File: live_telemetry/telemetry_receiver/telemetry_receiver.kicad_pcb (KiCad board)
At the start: 2 copper layers, 52.5 x 30.7 mm, 20 parts, among them J1 Conn_Coaxial, J2 Programming Header, J3 USB_A, U1 PIC16LF1455, U2 RFM95W, U3 AP2114H-3.3

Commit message: Address Aaron's comments on initial component layout
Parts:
- J1: footprint canhw_footprints:AmphenolRF_coaxial_conn_901-10510-2 -> canhw_footprints:RF_connector_SMA_3-1478978-1
- moved D3 10.7 mm to (124.3, 79.7), turned to 180 degrees
- moved R2 9.95 mm to (124.4, 76.3), turned to 180 degrees
- moved D2 8.03 mm to (131.6, 79.6), turned to 180 degrees
- moved R1 6.98 mm to (131.7, 76.3), turned to 180 degrees
- moved J1 5.87 mm to (151.8, 98.5)
- moved D1 5.61 mm to (138.9, 79.6), turned to 180 degrees
- moved J3 4.67 mm to (104.1, 88.5)
- moved J2 4.42 mm to (146.0, 76.4)
- moved R4 4.03 mm to (139.0, 76.3), turned to 180 degrees
- moved U2 3.80 mm to (128.1, 91.5)
- moved C3 1.69 mm to (144.3, 91.5)
- moved C1 1.61 mm to (140.3, 91.4)
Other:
- board size 52.5 x 30.7 mm -> 48.6 x 28 mm

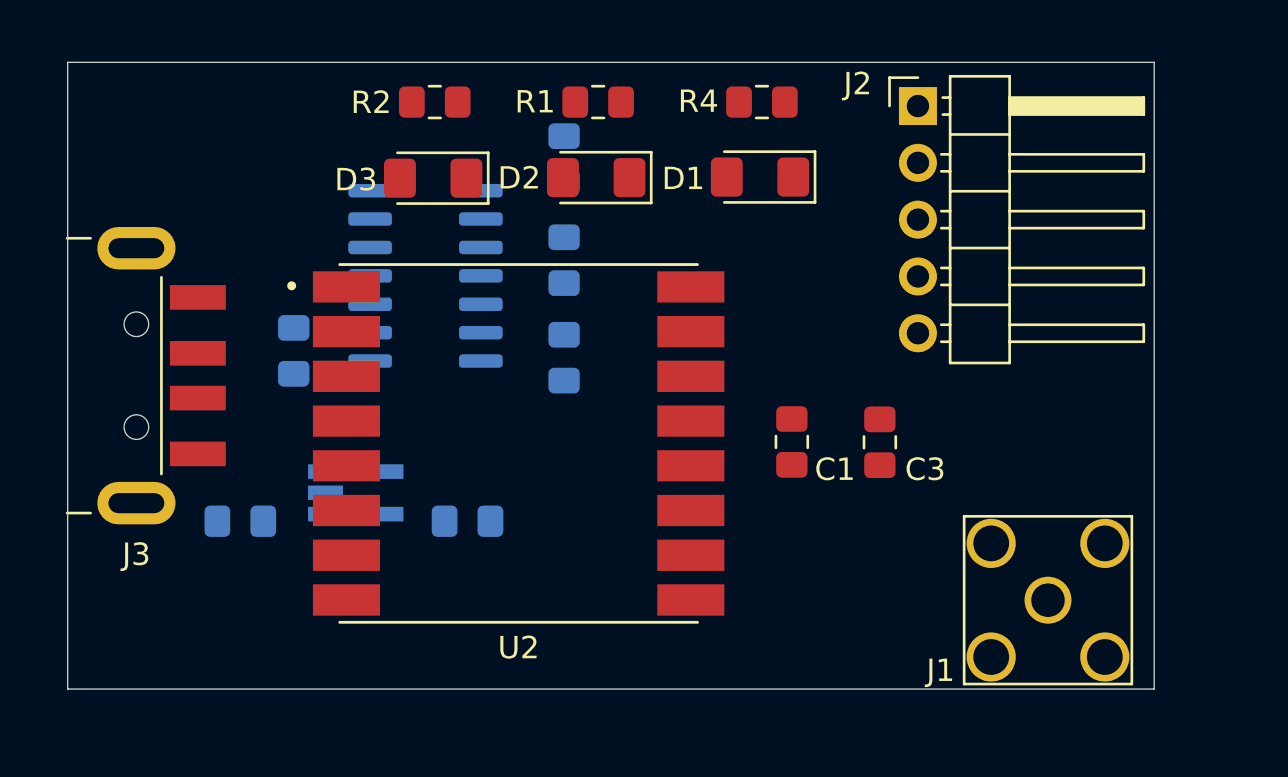
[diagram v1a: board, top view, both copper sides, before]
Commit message: Add initial trace routing
Note:
-LED colours still need to be added
-Waterloo Rocketry logo needs to be added with the board name and
my name on the right side of the board
-Copper pours will be added next commit
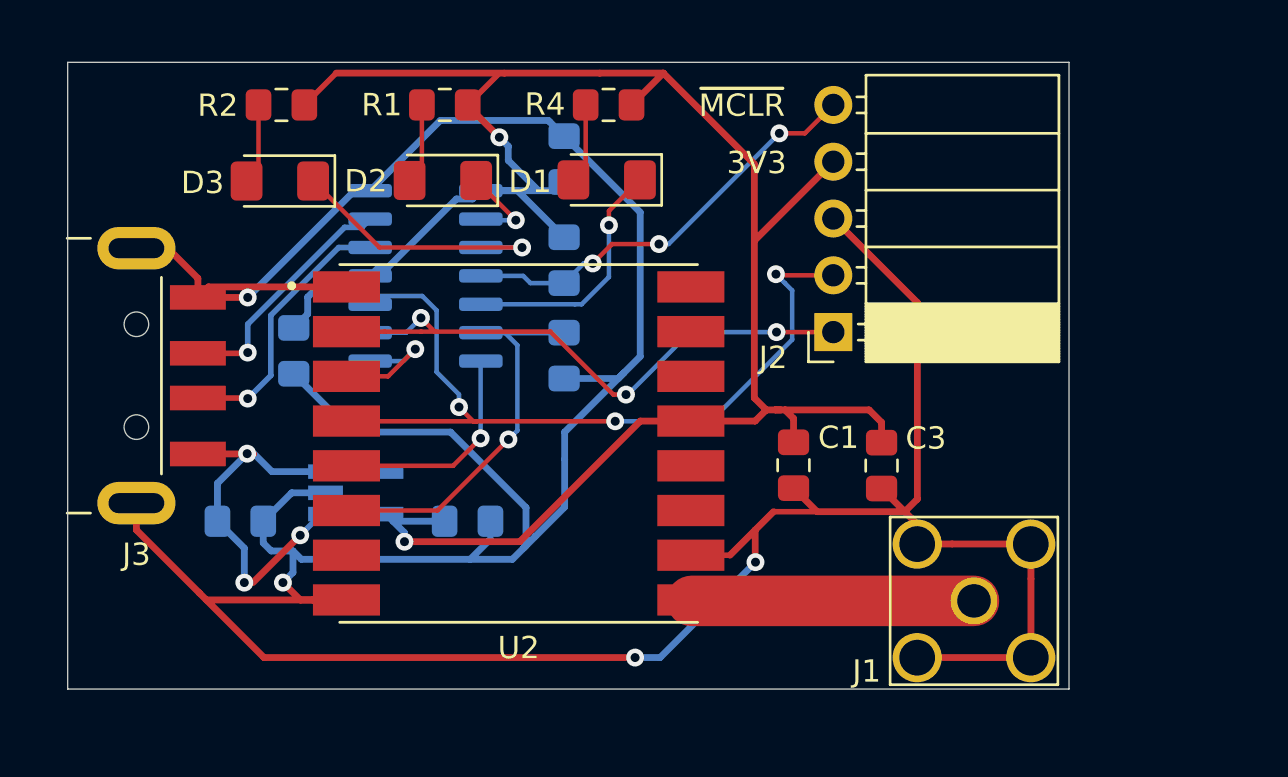
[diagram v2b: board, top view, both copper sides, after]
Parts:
- J2: footprint Connector_PinHeader_2.54mm:PinHeader_1x05_P2.54mm_Horizontal -> Connector_PinSocket_2.54mm:PinSocket_1x05_P2.54mm_Horizontal
- moved J2 10.8 mm to (142.2, 86.5), turned to 180 degrees
- moved D1 6.86 mm to (132.1, 79.7)
- moved R2 6.86 mm to (117.5, 76.4)
- moved R4 6.86 mm to (132.1, 76.4)
- moved D3 6.86 mm to (117.4, 79.8)
- moved D2 6.86 mm to (124.7, 79.8)
- moved R1 6.86 mm to (124.8, 76.4)
- moved J1 3.31 mm to (148.5, 98.6)
- moved C1 1.04 mm to (140.4, 92.5), turned to 270 degrees
- moved C3 1.04 mm to (144.3, 92.5), turned to 270 degrees
- moved R5 0.09 mm to (130.1, 87.6)
- turned R3 to 270 degrees
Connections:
- J2 pad 1: /ISCPCLK -> /ICSPCLK
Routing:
- net GND: track 0.00 -> 183.3 mm, vias 0 -> 4
- net +3V3: track 0.00 -> 98.9 mm, vias 0 -> 2
- net /ICSPDAT: track 0.00 -> 36.4 mm, vias 0 -> 3
- net /ICSPCLK: track 0.00 -> 27.6 mm, vias 0 -> 3
- net /~MCLR: track 0.00 -> 19.2 mm, vias 0 -> 3
- net /RESET: track 0.00 -> 18.5 mm, vias 0 -> 1
- net +5V: track 0.00 -> 17.8 mm, vias 0 -> 3
- net Net-(AE1-Pad1): track 0.00 -> 12.7 mm
- net Net-(D3-Pad1): track 0.00 -> 12.4 mm, vias 0 -> 1
- net /USB_D-: track 0.00 -> 12.1 mm, vias 0 -> 1
- net Net-(D1-Pad1): track 0.00 -> 11.2 mm, vias 0 -> 1
- net /USB_D+: track 0.00 -> 10.9 mm, vias 0 -> 1
- net /~SS: track 0.00 -> 9.97 mm, vias 0 -> 1
- net /MOSI: track 0.00 -> 5.82 mm, vias 0 -> 1
- net Net-(D2-Pad1): track 0.00 -> 4.10 mm, vias 0 -> 1
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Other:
- board size 48.6 x 28 mm -> 44.8 x 28 mm
- net class Default: trace_width 0.25 -> 0.2032
- net class Power added: clearance 0.2, trace_width 0.3048, via_dia 0.8, via_drill 0.4
- board text added: "3V3"
- board text added: "~MCLR"

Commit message: Add copper pours and address Jared's comments
Note:
-Still haven't fixed CAN TX/RX lines running through OSC1&2
-Still need to add team logo
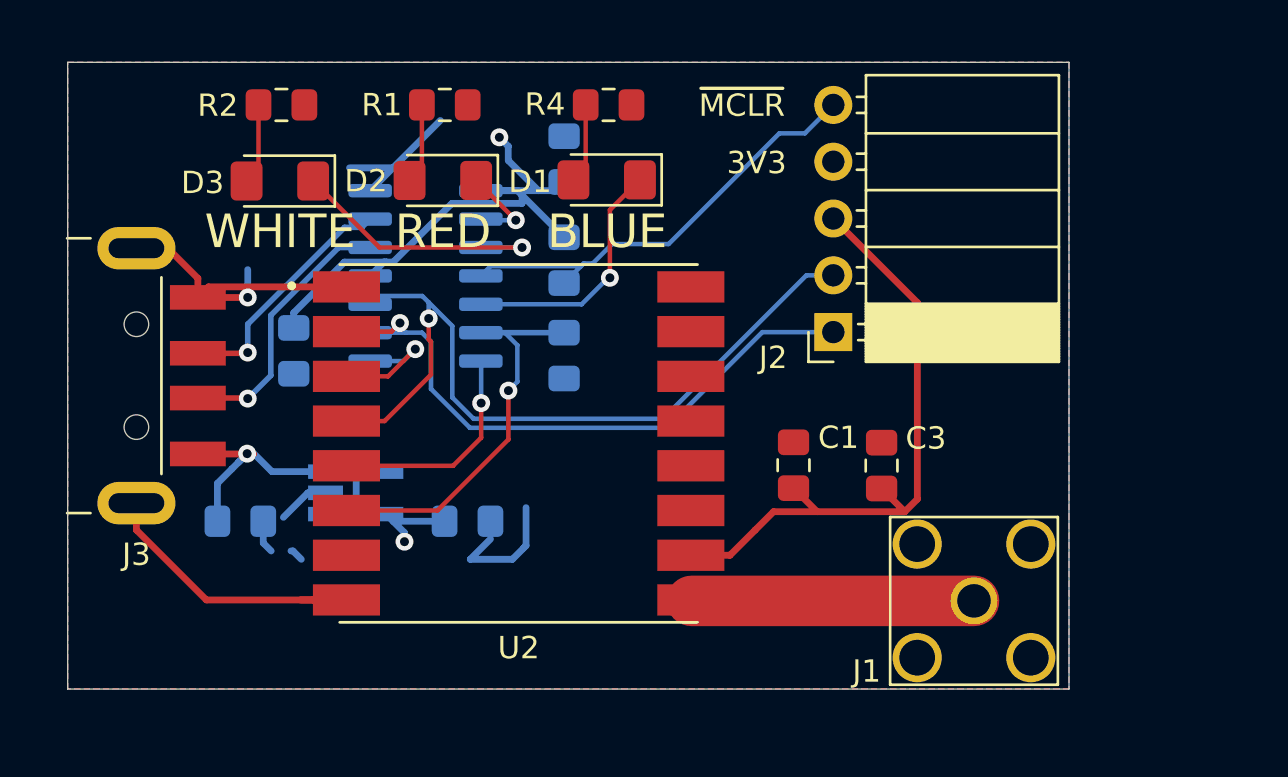
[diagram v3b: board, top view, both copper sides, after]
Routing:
- net GND: track 183.3 -> 77.6 mm, vias 4 -> 1
- net +3V3: track 98.9 -> 30.2 mm
- net +5V: track 17.8 -> 14.7 mm, vias 3 -> 1
- net /ICSPCLK: track 27.6 -> 28.6 mm, vias 3 -> 1
- net /ICSPDAT: track 36.4 -> 35.6 mm, vias 3 -> 1
- net /~MCLR: track 19.2 -> 20.0 mm, vias 3 -> 0
- added copper zone on F.Cu, net +3V3
- added copper zone on B.Cu, net GND
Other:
- board text added: "BLUE"
- board text added: "RED"
- board text added: "WHITE"

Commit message: Address Aaron's comments
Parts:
- moved C6 1.54 mm to (127.2, 95.8), turned to 270 degrees
- moved C5 1.38 mm to (114.6, 95.8), turned to 270 degrees
- moved C2 1.22 mm to (131.4, 78.8)
- moved R3 1.22 mm to (131.4, 83.3)
- moved R5 1.22 mm to (131.4, 87.6)
- moved C4 1.14 mm to (116.9, 87.4)
- moved J3 0.94 mm to (103.2, 88.5)
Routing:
- net GND: track 77.6 -> 67.3 mm, vias 1 -> 2
- net +3V3: track 30.2 -> 35.6 mm
- net Net-(D1-Pad1): track 11.2 -> 12.8 mm
- net /USB_D+: track 10.9 -> 11.9 mm
- net /USB_D-: track 12.1 -> 13.0 mm
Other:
- board size 44.8 x 28 mm -> 45.7 x 28 mm

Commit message: Address Alex's comments
Note:
-Still need to pick names for the boards
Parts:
- added G***: LOGO, Team logo:Logo_SilkScreen_5mm, B.Cu at (138.7, 92.5)
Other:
- board text added: "*INSERT NAME* D. Kletke 2020-02-23"

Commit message: Add isolated ground pours for RF modules
Note:
-Still trying to come up with names
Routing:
- net GND: track 67.3 -> 13.9 mm, vias 2 -> 39
- net +3V3: track 35.6 -> 46.9 mm
- added copper zone on F.Cu, net GND
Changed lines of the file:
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@@
     (thickness 1.6)
     (drawings 12)
-    (tracks 186)
+    (tracks 202)
     (zones 0)
     (modules 21)
@@
     (36 B.SilkS user)
     (37 F.SilkS user)
-    (38 B.Mask user hide)
-    (39 F.Mask user hide)
+    (38 B.Mask user)
+    (39 F.Mask user)
     (40 Dwgs.User user)
     (41 Cmts.User user hide)
@@
   (gr_line (start 107.0102 102.5144) (end 107.0102 74.56) (layer Edge.Cuts) (width 0.05))
   (segment (start 145.9484 95.132) (end 145.9484 96.012) (width 0.25) (layer F.Cu) (net 1))
-  (segment (start 141.4645 94.5687) (end 140.4112 93.5154) (width 0.3048) (layer F.Cu) (net 1))
-  (segment (start 145.3851 94.5687) (end 141.4645 94.5687) (width 0.3048) (layer F.Cu) (net 1))
-  (segment (start 144.3482 93.5318) (end 145.3851 94.5687) (width 0.3048) (layer F.Cu) (net 1))
-  (segment (start 145.9484 94.0054) (end 145.3851 94.5687) (width 0.3048) (layer F.Cu) (net 1))
-  (segment (start 145.9484 85.217) (end 145.9484 94.0054) (width 0.3048) (layer F.Cu) (net 1))
-  (segment (start 142.1892 81.4578) (end 145.9484 85.217) (width 0.3048) (layer F.Cu) (net 1))
-  (segment (start 139.5151 94.5687) (end 141.4645 94.5687) (width 0.3048) (layer F.Cu) (net 1))
   (segment (start 135.8176 96.5162) (end 137.5676 96.5162) (width 0.3048) (layer F.Cu) (net 1))
   (via (at 114.9096 85.0138) (size 0.8) (drill 0.4) (layers F.Cu B.Cu) (net 1))
   (segment (start 113.7754 84.9884) (end 113.7734 84.9864) (width 0.3048) (layer F.Cu) (net 1))
   (segment (start 120.4176 98.5162) (end 118.9124 98.5162) (width 0.3048) (layer F.Cu) (net 1))
-  (segment (start 138.6954 95.3884) (end 139.5151 94.5687) (width 0.3048) (layer F.Cu) (net 1))
-  (segment (start 137.5676 96.5162) (end 138.6954 95.3884) (width 0.3048) (layer F.Cu) (net 1))
   (segment (start 112.1384 94.1786) (end 110.0836 94.1786) (width 0.3048) (layer F.Cu) (net 1))
-  (segment (start 120.4176 98.5162) (end 116.476 98.5162) (width 0.3048) (layer F.Cu) (net 1))
-  (via (at 115.3668 99.2378) (size 0.8) (drill 0.4) (layers F.Cu B.Cu) (net 1))
-  (segment (start 115.9012 98.7034) (end 115.3668 99.2378) (width 0.3048) (layer F.Cu) (net 1))
-  (segment (start 115.9012 97.9414) (end 115.9012 98.7034) (width 0.3048) (layer F.Cu) (net 1))
-  (segment (start 115.9012 97.9414) (end 112.1384 94.1786) (width 0.3048) (layer F.Cu) (net 1))
-  (segment (start 116.476 98.5162) (end 115.9012 97.9414) (width 0.3048) (layer F.Cu) (net 1))
   (segment (start 110.0836 82.7786) (end 112.6744 82.7786) (width 0.3048) (layer F.Cu) (net 1))
   (segment (start 113.0358 83.9216) (end 113.8174 83.9216) (width 0.3048) (layer F.Cu) (net 1))
@@
   (segment (start 112.6744 82.7786) (end 113.8174 83.9216) (width 0.3048) (layer F.Cu) (net 1))
   (segment (start 113.8174 83.9216) (end 114.9096 85.0138) (width 0.3048) (layer F.Cu) (net 1))
-  (segment (start 126.3524 96.8084) (end 127.1524 96.8084) (width 0.3048) (layer B.Cu) (net 1))
-  (segment (start 122.574678 96.8084) (end 126.3524 96.8084) (width 0.3048) (layer B.Cu) (net 1))
-  (segment (start 121.049199 95.282921) (end 122.574678 96.8084) (width 0.3048) (layer B.Cu) (net 1))
-  (segment (start 121.049199 94.208799) (end 121.049199 95.282921) (width 0.3048) (layer B.Cu) (net 1))
-  (segment (start 120.5664 93.726) (end 121.049199 94.208799) (width 0.3048) (layer B.Cu) (net 1))
-  (segment (start 119.4816 93.726) (end 120.5664 93.726) (width 0.3048) (layer B.Cu) (net 1))
-  (segment (start 120.4176 84.5162) (end 115.966 84.5162) (width 0.3048) (layer F.Cu) (net 1))
-  (segment (start 115.966 84.5162) (end 115.443 85.0392) (width 0.3048) (layer F.Cu) (net 1))
   (segment (start 114.935 85.0392) (end 114.9096 85.0138) (width 0.3048) (layer F.Cu) (net 1))
-  (segment (start 115.443 85.0392) (end 114.935 85.0392) (width 0.3048) (layer F.Cu) (net 1))
+  (via (at 150.3426 98.5774) (size 0.8) (drill 0.4) (layers F.Cu B.Cu) (net 1))
+  (via (at 151.2316 98.5774) (size 0.8) (drill 0.4) (layers F.Cu B.Cu) (net 1))
+  (via (at 152.1206 98.5774) (size 0.8) (drill 0.4) (layers F.Cu B.Cu) (net 1))
+  (via (at 148.0058 96.647) (size 0.8) (drill 0.4) (layers F.Cu B.Cu) (net 1))
+  (via (at 148.971 96.7486) (size 0.8) (drill 0.4) (layers F.Cu B.Cu) (net 1))
+  (via (at 147.9804 100.457) (size 0.8) (drill 0.4) (layers F.Cu B.Cu) (net 1))
+  (via (at 148.971 100.3554) (size 0.8) (drill 0.4) (layers F.Cu B.Cu) (net 1))
+  (via (at 146.7358 93.0148) (size 0.8) (drill 0.4) (layers F.Cu B.Cu) (net 1))
+  (via (at 147.7772 93.0148) (size 0.8) (drill 0.4) (layers F.Cu B.Cu) (net 1))
+  (via (at 148.8186 93.0148) (size 0.8) (drill 0.4) (layers F.Cu B.Cu) (net 1))
+  (via (at 149.86 93.0148) (size 0.8) (drill 0.4) (layers F.Cu B.Cu) (net 1))
+  (via (at 150.9014 93.0148) (size 0.8) (drill 0.4) (layers F.Cu B.Cu) (net 1))
+  (via (at 151.9174 93.0148) (size 0.8) (drill 0.4) (layers F.Cu B.Cu) (net 1))
+  (via (at 143.8148 101.7778) (size 0.8) (drill 0.4) (layers F.Cu B.Cu) (net 1))
+  (via (at 142.748 101.7778) (size 0.8) (drill 0.4) (layers F.Cu B.Cu) (net 1))
+  (via (at 141.6812 101.8032) (size 0.8) (drill 0.4) (layers F.Cu B.Cu) (net 1))
+  (via (at 140.6398 101.8032) (size 0.8) (drill 0.4) (layers F.Cu B.Cu) (net 1))
+  (via (at 139.5984 101.8032) (size 0.8) (drill 0.4) (layers F.Cu B.Cu) (net 1))
+  (via (at 138.557 101.8032) (size 0.8) (drill 0.4) (layers F.Cu B.Cu) (net 1))
+  (via (at 137.5156 101.8032) (size 0.8) (drill 0.4) (layers F.Cu B.Cu) (net 1))
+  (via (at 136.4742 101.8032) (size 0.8) (drill 0.4) (layers F.Cu B.Cu) (net 1))
+  (via (at 135.4328 101.8032) (size 0.8) (drill 0.4) (layers F.Cu B.Cu) (net 1))
+  (via (at 134.3914 101.8032) (size 0.8) (drill 0.4) (layers F.Cu B.Cu) (net 1))
+  (via (at 133.35 101.8032) (size 0.8) (drill 0.4) (layers F.Cu B.Cu) (net 1))
+  (via (at 132.2832 101.8032) (size 0.8) (drill 0.4) (layers F.Cu B.Cu) (net 1))
+  (via (at 131.2418 101.8032) (size 0.8) (drill 0.4) (layers F.Cu B.Cu) (net 1))
+  (via (at 130.2004 101.8032) (size 0.8) (drill 0.4) (layers F.Cu B.Cu) (net 1))
+  (via (at 129.159 101.8032) (size 0.8) (drill 0.4) (layers F.Cu B.Cu) (net 1))
+  (via (at 128.1176 101.8032) (size 0.8) (drill 0.4) (layers F.Cu B.Cu) (net 1))
+  (via (at 127.0762 101.8032) (size 0.8) (drill 0.4) (layers F.Cu B.Cu) (net 1))
+  (via (at 126.0348 101.8032) (size 0.8) (drill 0.4) (layers F.Cu B.Cu) (net 1))
+  (via (at 124.9934 101.8032) (size 0.8) (drill 0.4) (layers F.Cu B.Cu) (net 1))
+  (via (at 123.952 101.8032) (size 0.8) (drill 0.4) (layers F.Cu B.Cu) (net 1))
+  (via (at 122.9106 101.8286) (size 0.8) (drill 0.4) (layers F.Cu B.Cu) (net 1))
+  (via (at 121.8692 101.8286) (size 0.8) (drill 0.4) (layers F.Cu B.Cu) (net 1))
+  (via (at 120.8278 101.8286) (size 0.8) (drill 0.4) (layers F.Cu B.Cu) (net 1))
+  (via (at 119.7864 101.8032) (size 0.8) (drill 0.4) (layers F.Cu B.Cu) (net 1))
+  (via (at 118.745 101.8032) (size 0.8) (drill 0.4) (layers F.Cu B.Cu) (net 1))
   (segment (start 128.0668 80.2132) (end 126.427 80.2132) (width 0.3048) (layer B.Cu) (net 2))
   (via (at 127.254 77.8256) (size 0.8) (drill 0.4) (layers F.Cu B.Cu) (net 2))
@@
   (segment (start 122.264 94.7584) (end 122.1816 94.676) (width 0.3048) (layer B.Cu) (net 2))
   (segment (start 123.6054 94.7584) (end 122.264 94.7584) (width 0.3048) (layer B.Cu) (net 2))
-  (via (at 124.9426 95.4786) (size 0.8) (drill 0.4) (layers F.Cu B.Cu) (net 2))
-  (segment (start 124.2224 94.7584) (end 124.9426 95.4786) (width 0.3048) (layer B.Cu) (net 2))
   (segment (start 124.1716 94.7584) (end 124.2224 94.7584) (width 0.3048) (layer B.Cu) (net 2))
   (segment (start 124.1716 94.7584) (end 123.6054 94.7584) (width 0.3048) (layer B.Cu) (net 2))
-  (segment (start 127.1524 94.7584) (end 124.1716 94.7584) (width 0.3048) (layer B.Cu) (net 2))
   (segment (start 119.87059 83.40561) (end 122.20739 83.40561) (width 0.3048) (layer B.Cu) (net 2))
   (segment (start 116.9162 86.36) (end 119.87059 83.40561) (width 0.3048) (layer B.Cu) (net 2))
+  (via (at 114.9096 100.5332) (size 0.8) (drill 0.4) (layers F.Cu B.Cu) (net 2))
+  (segment (start 119.0752 100.5332) (end 114.9096 100.5332) (width 0.3048) (layer B.Cu) (net 2))
+  (segment (start 124.85 94.7584) (end 119.0752 100.5332) (width 0.3048) (layer B.Cu) (net 2))
+  (segment (start 124.85 94.7584) (end 124.1716 94.7584) (width 0.3048) (layer B.Cu) (net 2))
+  (segment (start 127.1524 94.7584) (end 124.85 94.7584) (width 0.3048) (layer B.Cu) (net 2))
   (segment (start 119.4816 94.676) (end 119.296875 94.676) (width 0.25) (layer B.Cu) (net 3))
   (segment (start 117.1756 93.4548) (end 115.883 93.4548) (width 0.3048) (layer B.Cu) (net 3))
@@
     )
   )
+  (zone (net 1) (net_name GND) (layer F.Cu) (hatch edge 0.508)
+    (connect_pads (clearance 0.1524))
+    (min_thickness 0.254)
+    (fill yes (arc_segments 32) (thermal_gap 0.508) (thermal_bridge_width 0.508))
+    (polygon
+      (pts
+        (xy 152.7302 92.5322) (xy 134.0866 92.5322) (xy 134.0866 83.3628) (xy 118.0338 83.3628) (xy 118.0338 99.7458)
+        (xy 118.0338 102.5144) (xy 152.7302 102.5144)
+      )
+    )
+  )
   (zone (net 2) (net_name +3V3) (layer F.Cu) (hatch edge 0.508)
     (connect_pads (clearance 0.1524))
@@
     (polygon
       (pts
-        (xy 107.0102 74.549) (xy 107.0102 102.5144) (xy 152.7302 102.5144) (xy 152.7302 74.549)
+        (xy 152.7302 92.3036) (xy 134.62 92.3036) (xy 134.62 83.0326) (xy 117.6528 83.0326) (xy 117.6528 102.5144)
+        (xy 107.0102 102.5144) (xy 107.0102 74.5744) (xy 152.7302 74.5744) (xy 152.7302 92.2782)
       )
     )

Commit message: Add board names
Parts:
- moved G*** 1.17 mm to (137.6, 92.8)
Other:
- board text added: "Kyoto D. Kletke 2020-02-23"
- board text removed: "*INSERT NAME* D. Kletke 2020-02-23"
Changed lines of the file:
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@@
   )
   (module "Team logo:Logo_SilkScreen_5mm" (layer B.Cu)
-    (at 138.7094 92.5322 180)
+    (at 137.5664 92.7608 180)
     (fp_text reference G*** (at 0 0) (layer B.SilkS) hide
       (effects (font (size 1.524 1.524) (thickness 0.3)) (justify mirror))
@@
     (descr "Through hole angled socket strip, 1x05, 2.54mm pitch, 8.51mm socket length, single row (from Kicad 4.0.7), script generated")
     (tags "Through hole angled socket strip THT 1x05 2.54mm single row")
-    (fp_text reference J2 (at 2.6924 -1.143) (layer F.SilkS)
+    (fp_text reference J2 (at -9.3472 -2.2606) (layer F.SilkS)
       (effects (font (size 1 1) (thickness 0.15)))
     )
@@
     )
   )
-  (gr_text "*INSERT NAME*\nD. Kletke\n2020-02-23" (at 138.5824 97.7138) (layer B.SilkS)
+  (gr_text "Kyoto\nD. Kletke\n2020-02-23" (at 137.4902 97.7646) (layer B.SilkS)
     (effects (font (size 1 1) (thickness 0.15)) (justify mirror))
   )
@@
   )
   (gr_text WHITE (at 117.4496 82.042) (layer F.SilkS)
-    (effects (font (size 1.5 1.5) (thickness 0.3)))
+    (effects (font (size 1 1) (thickness 0.15)))
   )
   (gr_text BLUE (at 132.08 82.042) (layer F.SilkS)
-    (effects (font (size 1.5 1.5) (thickness 0.3)))
+    (effects (font (size 1 1) (thickness 0.15)))
   )
   (gr_text RED (at 124.7394 82.042) (layer F.SilkS)
-    (effects (font (size 1.5 1.5) (thickness 0.3)))
-  )
-  (gr_text 3V3 (at 138.7602 78.9686) (layer F.SilkS)
     (effects (font (size 1 1) (thickness 0.15)))
   )
-  (gr_text ~MCLR (at 138.0998 76.4032) (layer F.SilkS)
+  (gr_text 3V3 (at 139.065 78.8416) (layer F.SilkS)
     (effects (font (size 1 1) (thickness 0.15)))
   )
+  (gr_text ~MCLR (at 138.4046 76.6064) (layer F.SilkS)
+    (effects (font (size 1 1) (thickness 0.15)))
+  )
